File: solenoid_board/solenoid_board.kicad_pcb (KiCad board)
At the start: 2 copper layers, 151.1 x 63.5 mm, 207 parts, among them J1 output, J10 output, J11 output, J12 PORT, J13 PORT, J14 PORT, J15 PORT, J16 PORT, J17 PORT, J18 PORT, J19 PORT, J2 Conn_02x13_Odd_Even, J20 5V in, J21 XT60-M, J3 output, J4 output, J5 output, J6 output, J7 output, J8 output, J9 output, Q1 AOD4184A, Q10 AOD4184A, Q2 AOD4184A, Q3 AOD4184A, Q4 AOD4184A, Q5 AOD4184A, Q6 AOD4184A, Q7 AOD4184A, Q8 AOD4184A, Q9 AOD4184A, SW1 SW_Push, SW10 SW_Push, SW2 SW_Push, SW3 SW_Push, SW4 SW_Push, SW5 SW_Push, SW6 SW_Push, SW7 SW_Push, SW8 SW_Push, SW9 SW_Push, U1 EL357N, U10 EL357N, U11 EL357N, U12 EL357N, U13 EL357N, U14 EL357N, U15 EL357N, U16 EL357N, U17 EL357N, U18 EL357N, U2 EL357N, U3 EL357N, U4 EL357N, U5 EL357N, U6 EL357N, U7 EL357N, U8 EL357N, U9 EL357N

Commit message: test
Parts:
- removed J20: 5V in, Connector_BarrelJack:BarrelJack_GCT_DCJ200-10-A_Horizontal
- J21: footprint PolyuRobotics:XT60PW-M20 -> Connector_AMASS:AMASS_XT60-M_1x02_P7.20mm_Vertical
- moved J2 134.0 mm to (117.6, 90.2), turned to 180 degrees
- moved D22 20.3 mm to (222.2, 91.0)
- moved D16 20.3 mm to (209.6, 90.8)
- moved D3 20.3 mm to (146.1, 90.8)
- moved D13 20.3 mm to (184.2, 90.8)
- moved D15 20.3 mm to (196.8, 90.8)
- moved D2 20.3 mm to (133.3, 90.8)
- moved D24 20.3 mm to (234.9, 90.8)
- moved D25 20.3 mm to (247.7, 90.8)
- moved D5 20.3 mm to (158.8, 90.8)
- moved D7 20.3 mm to (171.4, 90.8)
- moved J12 16.0 mm to (149.6, 46.4), turned to 180 degrees
- moved J13 16.0 mm to (163.5, 46.4), turned to 180 degrees
- moved J14 16.0 mm to (177.5, 46.4), turned to 180 degrees
- moved J15 16.0 mm to (191.5, 46.4), turned to 180 degrees
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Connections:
- C1 pad 2: PB2 -> PA9
- C2 pad 2: PA9 -> PB2
- C3 pad 2: PA7 -> PB1
- C5 pad 2: PC11 -> PA5
- C6 pad 2: PB1 -> PA7
- C7 pad 2: PA5 -> PC11
- J21 pad 1: +24V -> GNDPWR
- J21 pad 2: GNDPWR -> +24V
- R10 pad 1: PB1 -> PA7
- R29 pad 1: PC11 -> PA5
- R30 pad 1: PA5 -> PC11
- R5 pad 1: PB2 -> PA9
- R64 pad 2: PB0 -> PB7
- R7 pad 1: PA9 -> PB2
- R74 pad 2: PC1 -> PC14
- R75 pad 2: PC0 -> PC15
- R8 pad 1: PA7 -> PB1
- R90 pad 2: PC15 -> PC0
- R91 pad 2: PC14 -> PC1
- R92 pad 2: PB7 -> PB0
- SW1 pad 2: PB1 -> PA7
- SW2 pad 2: PB2 -> PA9
- SW3 pad 2: PA9 -> PB2
- SW4 pad 2: PA7 -> PB1
- SW6 pad 2: PC11 -> PA5
- SW7 pad 2: PA5 -> PC11
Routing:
- net +5V: track 0.00 -> 219.1 mm
- net PB0: track 0.00 -> 138.2 mm, vias 0 -> 1
- net PA4: track 7.80 -> 143.9 mm
- net PC1: track 0.00 -> 125.3 mm, vias 0 -> 1
- net PC12: track 7.43 -> 131.9 mm
- net PC0: track 0.00 -> 111.7 mm, vias 0 -> 1
- net PC10: track 7.16 -> 117.5 mm
- net PC3: track 0.00 -> 105.9 mm, vias 0 -> 1
- net PC11: track 7.53 -> 107.0 mm
- net PC2: track 0.00 -> 93.5 mm, vias 0 -> 1
- net PA5: track 7.53 -> 96.2 mm
- net PC15: track 0.00 -> 84.5 mm, vias 0 -> 1
- net PA6: track 7.70 -> 85.1 mm
- net PB1: track 7.70 -> 81.5 mm
- net PC14: track 0.00 -> 73.5 mm, vias 0 -> 1
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- added copper zone on F.Cu, net GND
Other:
- board size 151.1 x 63.5 mm -> 146.1 x 63.5 mm

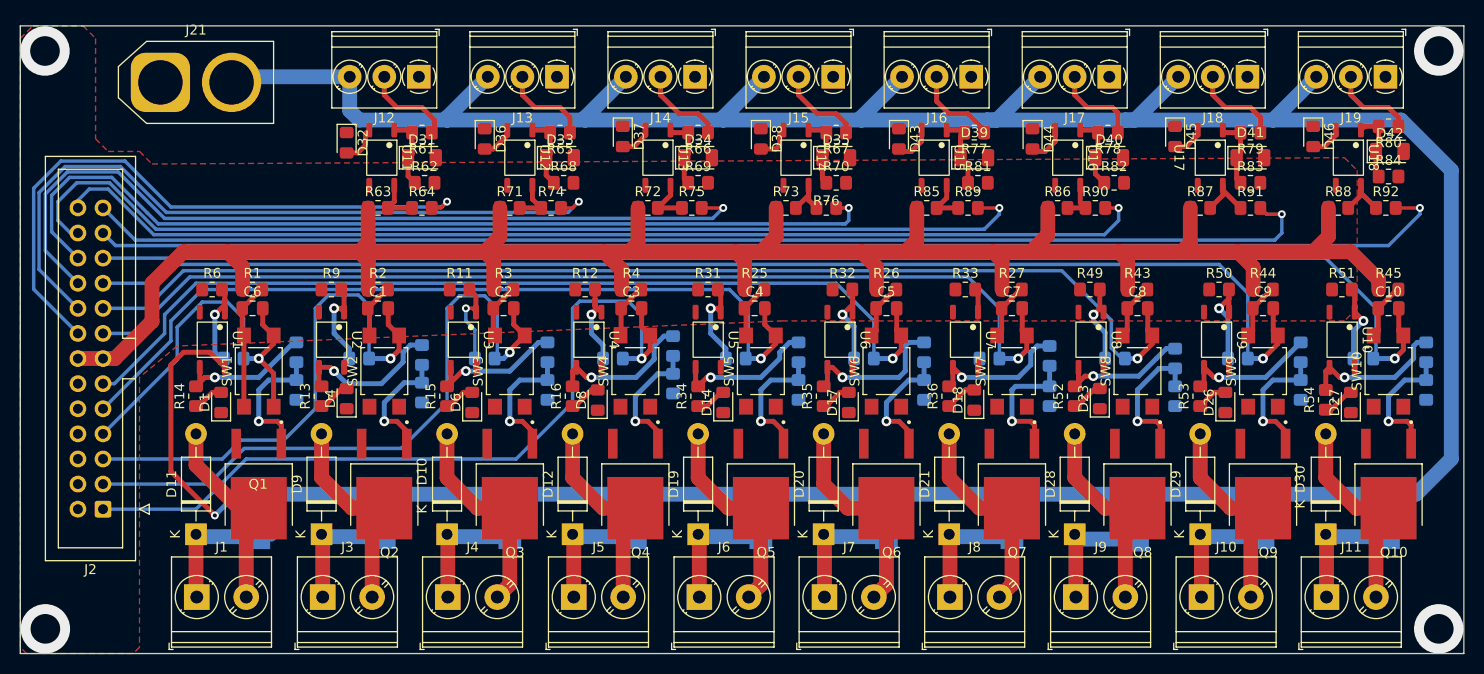
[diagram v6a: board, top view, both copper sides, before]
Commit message: power connector added
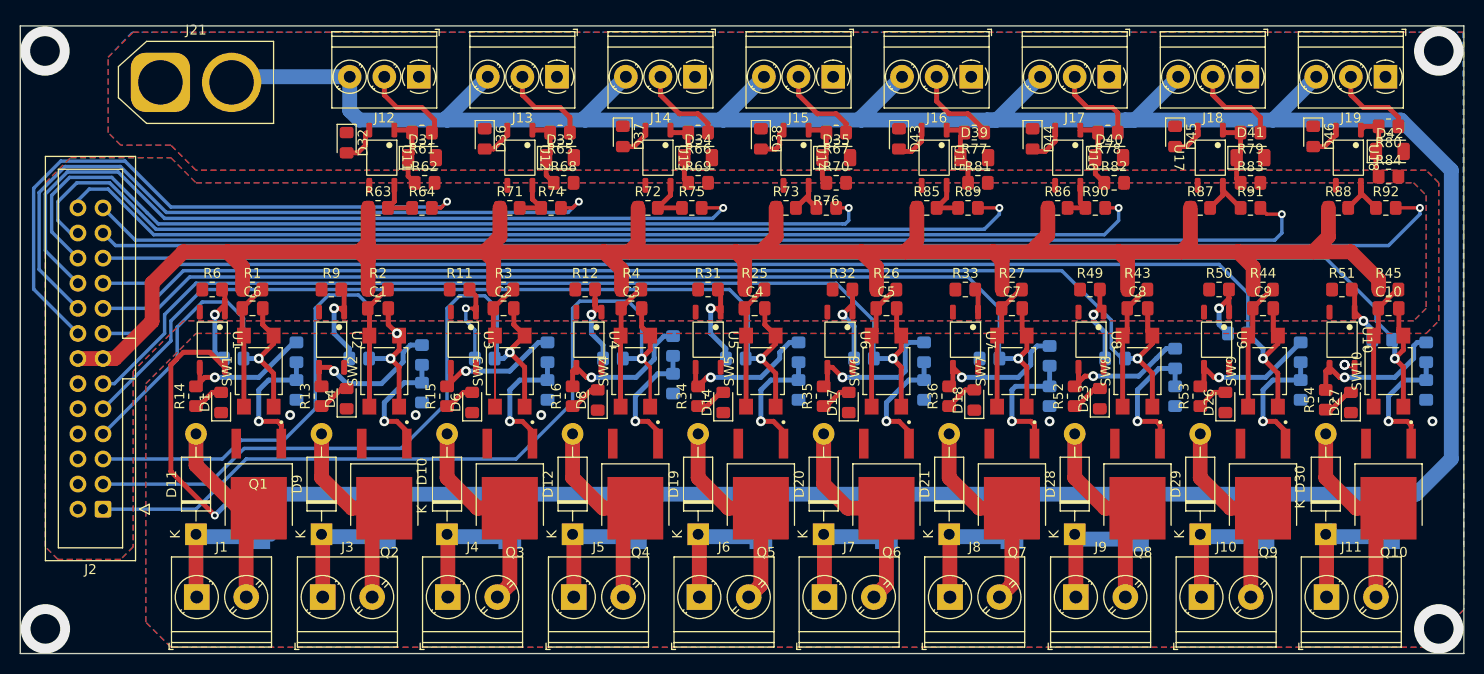
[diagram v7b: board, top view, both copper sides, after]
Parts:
- moved R48 2.69 mm to (247.0, 73.0)
- moved R47 2.54 mm to (232.4, 72.4)
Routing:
- net Net-(C3-Pad1): track 5.60 -> 13.1 mm
- net Net-(C9-Pad1): track 5.77 -> 13.0 mm
- net Net-(C8-Pad1): track 5.77 -> 13.0 mm
- net Net-(C5-Pad1): track 5.77 -> 13.0 mm
- net Net-(C10-Pad1): track 5.77 -> 13.0 mm
- net Net-(C7-Pad1): track 5.77 -> 13.0 mm
- net Net-(C1-Pad1): track 5.65 -> 12.8 mm
- net Net-(C4-Pad1): track 5.65 -> 12.8 mm
- net Net-(C2-Pad1): track 5.65 -> 12.8 mm
- net PB2: track 66.3 -> 72.4 mm
- net PC10: track 117.5 -> 123.0 mm
- net PA6: track 85.1 -> 90.6 mm
- net PC11: track 107.0 -> 112.2 mm
- net PA9: track 53.6 -> 58.8 mm, vias 1 -> 2
- net PB1: track 81.5 -> 86.7 mm
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- added copper zone on B.Cu, net GND
- added copper zone on B.Cu, net GNDPWR
- added copper zone on F.Cu, net GNDPWR

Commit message: update
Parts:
- moved R32 1.40 mm to (191.0, 67.9)
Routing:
- net +5V: track 219.1 -> 229.3 mm
- net Net-(R29-Pad2): track 8.66 -> 9.30 mm
- net GND: vias 0 -> 23
